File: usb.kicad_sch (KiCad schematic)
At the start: 46 parts, among them J901 AU-Y1008-2-BLK, J902 AU-Y1008-2-BLK, U901 USB2514B/M2, U902 AP22966DC8-7, U903 AP22966DC8-7, U904 USBLC6-2SC6, U905 USBLC6-2SC6, U906 USBLC6-2SC6, U907 USBLC6-2SC6, Y901 24 MHz

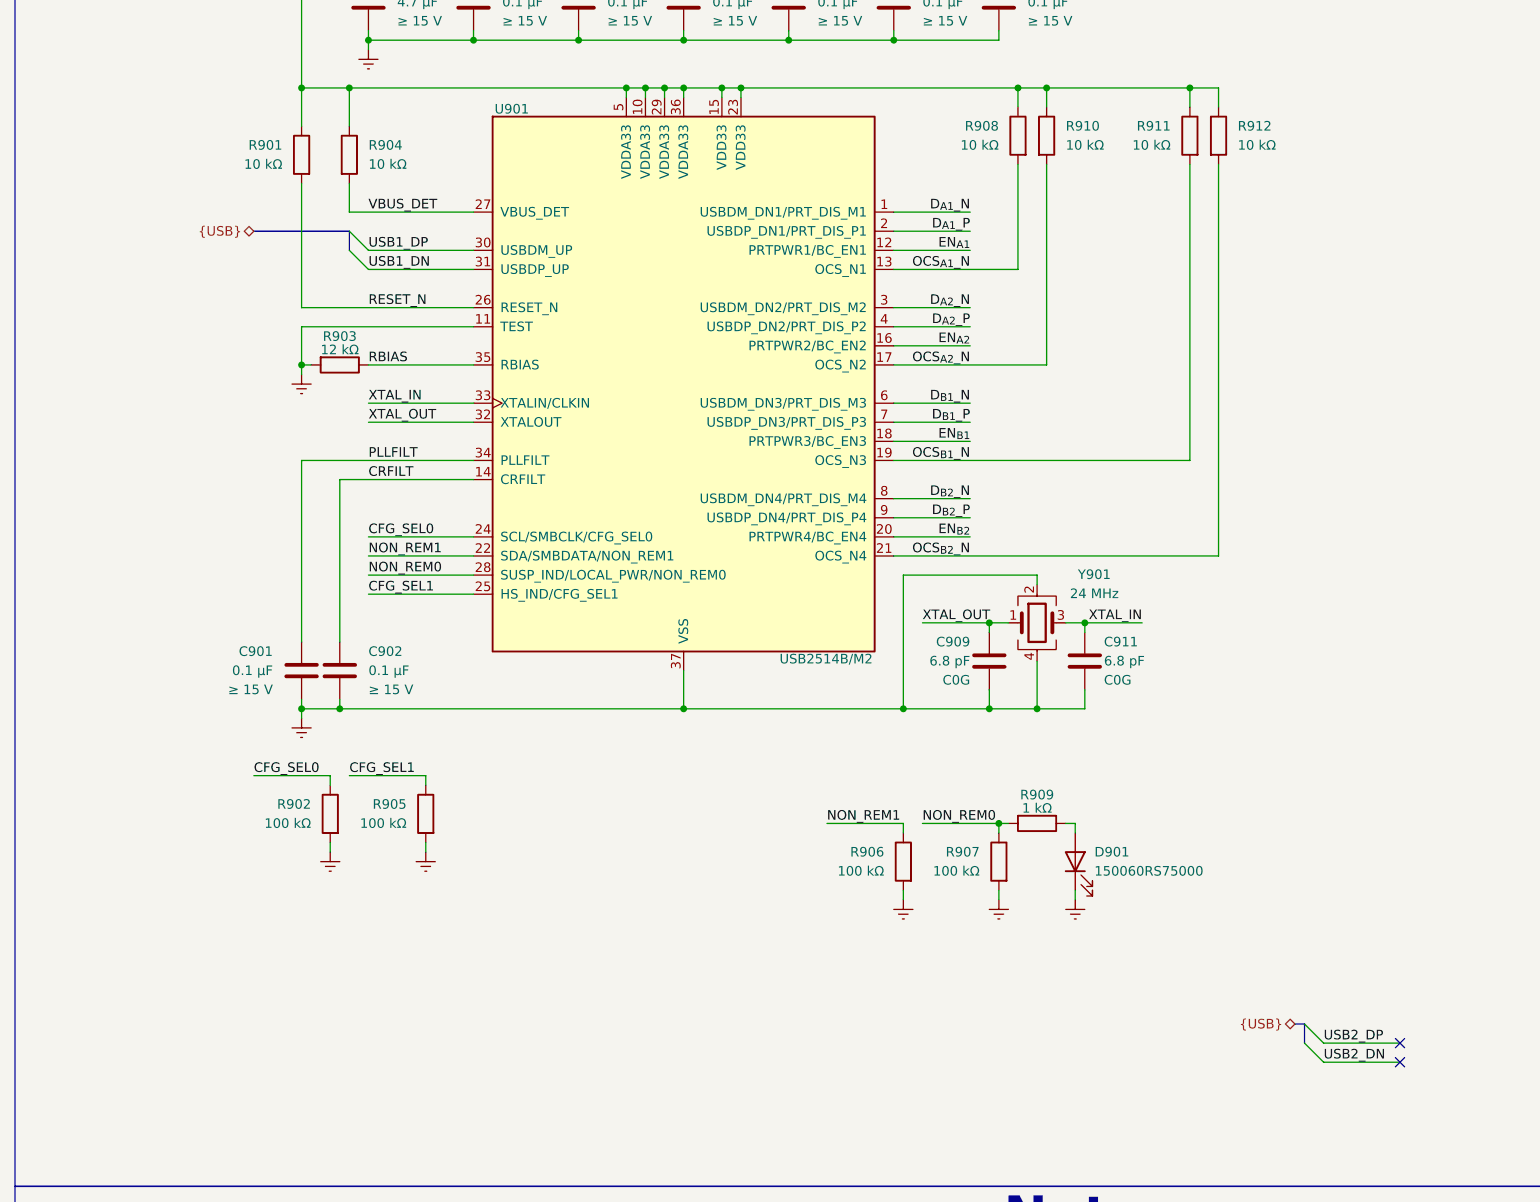
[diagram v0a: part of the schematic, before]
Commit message: Add ETH schema
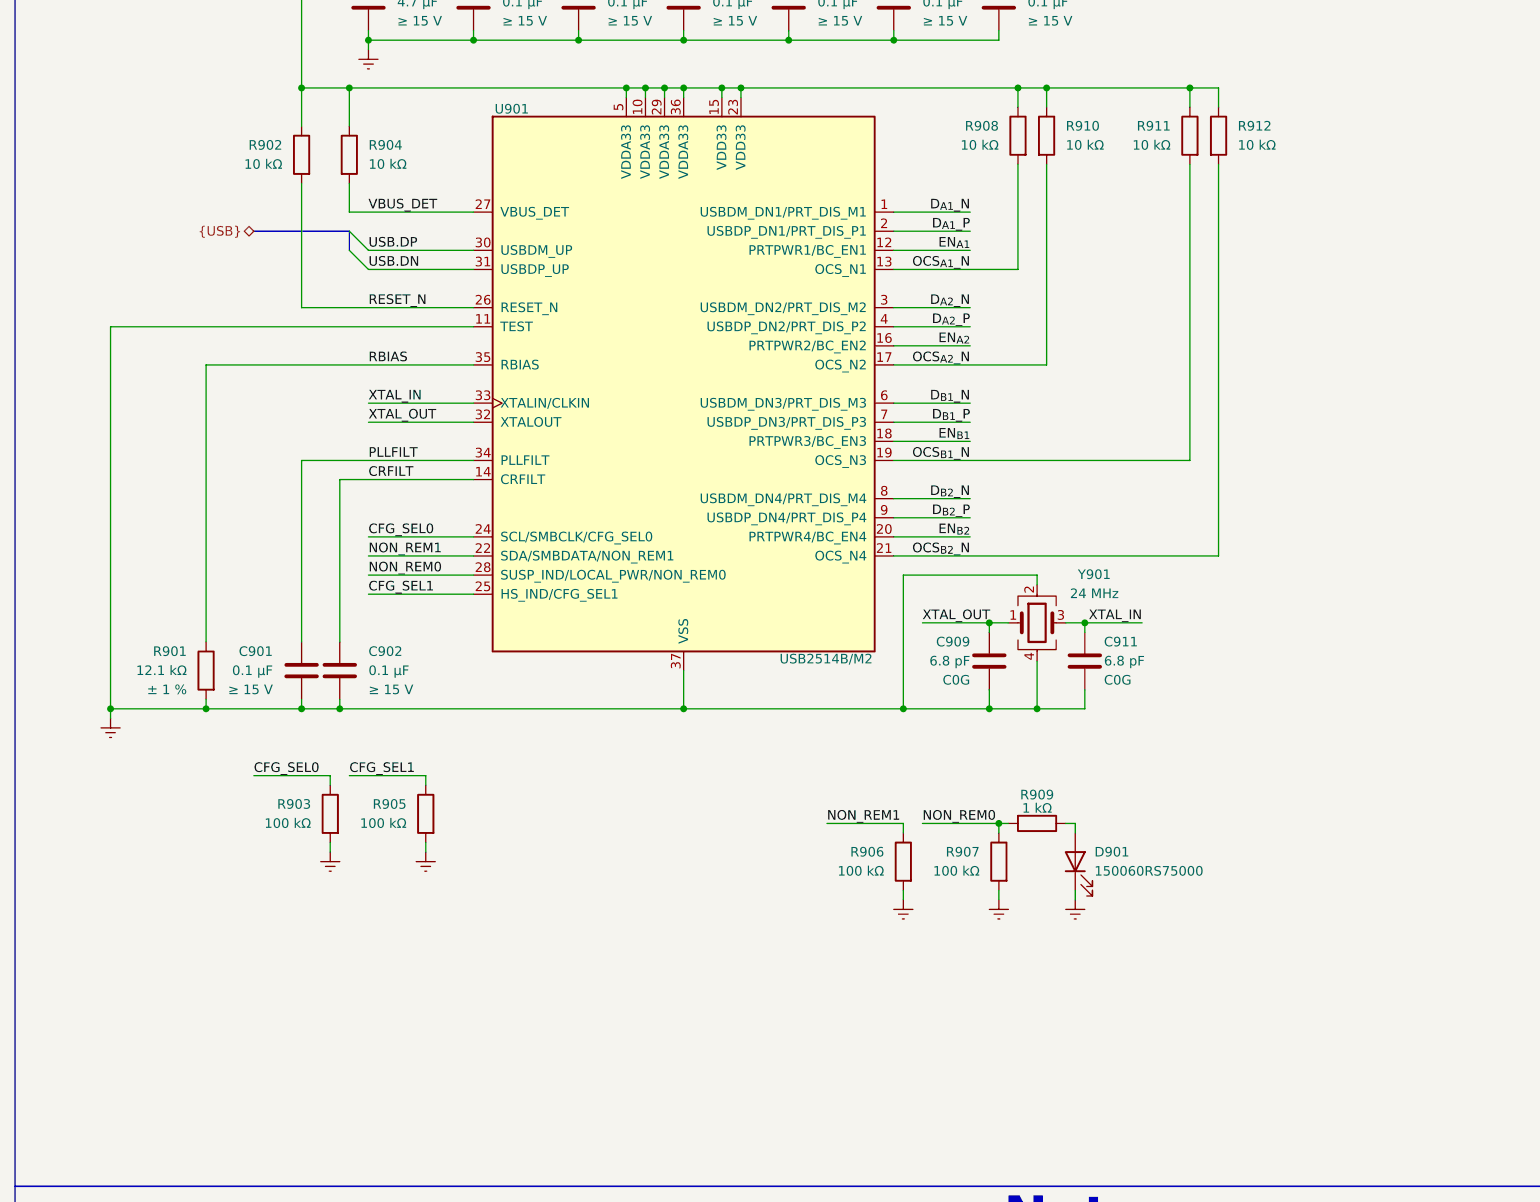
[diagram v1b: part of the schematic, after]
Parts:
- removed R903: 12 kΩ, perfect_footprints:R_0402_1005Metric, symbol Device:R
- added R901: 12.1 kΩ, perfect_footprints:R_0402_1005Metric, symbol Device:R
- renumbered R901 to R902, R902 to R903
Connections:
- net GND: now also R901.2
- net RBIAS: now also R901.1
- net USB1_DN renamed USB.DN
- net USB1_DP renamed USB.DP
- no-connect marks 4 -> 2

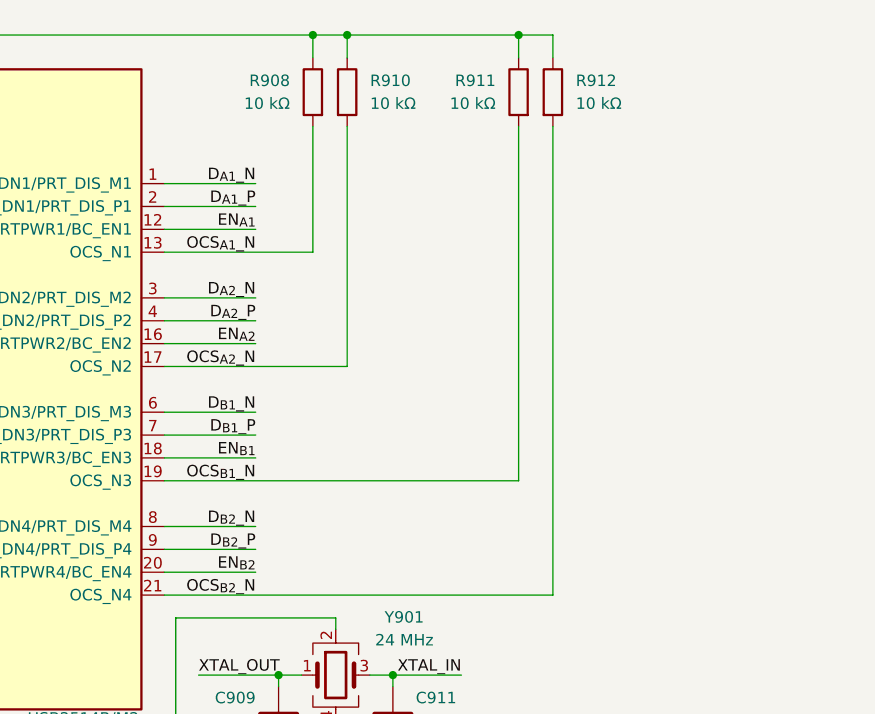
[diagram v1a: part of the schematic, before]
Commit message: Add series termination, assign netclasses, fill schemas' descriptions
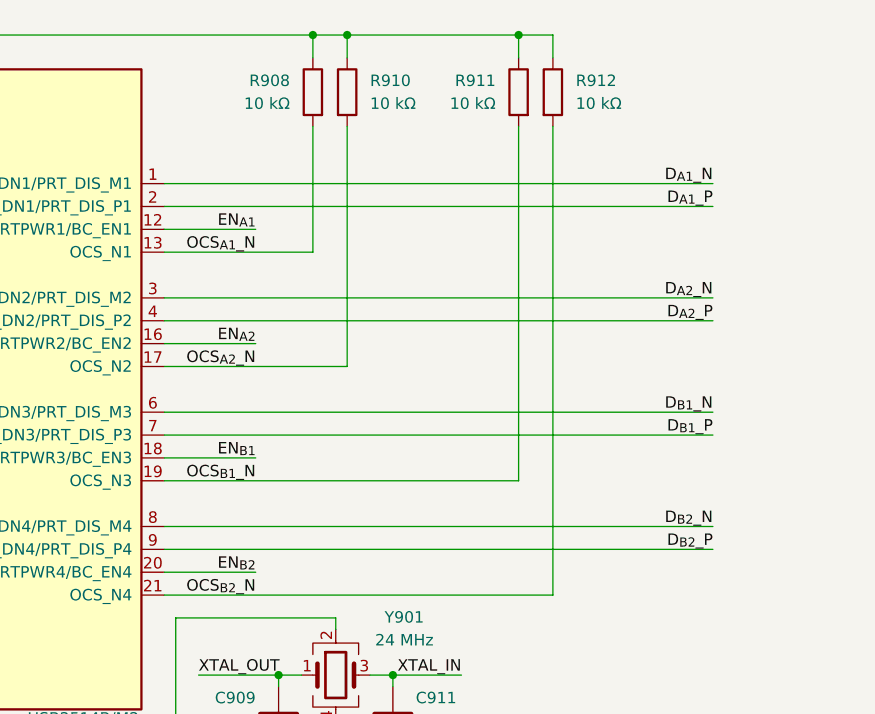
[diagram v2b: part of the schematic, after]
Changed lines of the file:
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@@
 	(wire
 		(pts
-			(xy 129.54 160.02) (xy 139.7 160.02)
+			(xy 129.54 160.02) (xy 190.5 160.02)
 		)
 		(stroke
@@
 	(wire
 		(pts
-			(xy 129.54 149.86) (xy 139.7 149.86)
+			(xy 129.54 149.86) (xy 190.5 149.86)
 		)
 		(stroke
@@
 	(wire
 		(pts
-			(xy 129.54 134.62) (xy 139.7 134.62)
+			(xy 129.54 134.62) (xy 190.5 134.62)
 		)
 		(stroke
@@
 	(wire
 		(pts
-			(xy 129.54 162.56) (xy 139.7 162.56)
+			(xy 129.54 162.56) (xy 190.5 162.56)
 		)
 		(stroke
@@
 	(wire
 		(pts
-			(xy 129.54 124.46) (xy 139.7 124.46)
+			(xy 129.54 124.46) (xy 190.5 124.46)
 		)
 		(stroke
@@
 	(wire
 		(pts
-			(xy 129.54 121.92) (xy 139.7 121.92)
+			(xy 129.54 121.92) (xy 190.5 121.92)
 		)
 		(stroke
@@
 	(wire
 		(pts
-			(xy 129.54 147.32) (xy 139.7 147.32)
+			(xy 129.54 147.32) (xy 190.5 147.32)
 		)
 		(stroke
@@
 	(wire
 		(pts
-			(xy 129.54 137.16) (xy 139.7 137.16)
+			(xy 129.54 137.16) (xy 190.5 137.16)
 		)
 		(stroke
@@
 	)
 	(label "D_{A1}_N"
-		(at 139.7 121.92 180)
+		(at 190.5 121.92 180)
 		(effects
 			(font
@@
 	)
 	(label "D_{B2}_P"
-		(at 139.7 162.56 180)
+		(at 190.5 162.56 180)
 		(effects
 			(font
@@
 	)
 	(label "D_{B2}_N"
-		(at 139.7 160.02 180)
+		(at 190.5 160.02 180)
 		(effects
 			(font
@@
 	)
 	(label "D_{A2}_N"
-		(at 139.7 134.62 180)
+		(at 190.5 134.62 180)
 		(effects
 			(font
@@
 	)
 	(label "D_{B1}_N"
-		(at 139.7 147.32 180)
+		(at 190.5 147.32 180)
 		(effects
 			(font
@@
 	)
 	(label "D_{A1}_P"
-		(at 139.7 124.46 180)
+		(at 190.5 124.46 180)
 		(effects
 			(font
@@
 	)
 	(label "D_{A2}_P"
-		(at 139.7 137.16 180)
+		(at 190.5 137.16 180)
 		(effects
 			(font
@@
 	)
 	(label "D_{B1}_P"
-		(at 139.7 149.86 180)
+		(at 190.5 149.86 180)
 		(effects
 			(font
@@
 		)
 	)
+	(rule_area
+		(polyline
+			(pts
+				(xy 176.53 119.38) (xy 176.53 163.83) (xy 179.07 163.83) (xy 179.07 119.38)
+			)
+			(stroke
+				(width 0)
+				(type dash)
+			)
+			(fill
+				(type none)
+			)
+		)
+	)
+	(rule_area
+		(polyline
+			(pts
+				(xy 347.98 166.37) (xy 347.98 181.61) (xy 350.52 181.61) (xy 350.52 166.37)
+			)
+			(stroke
+				(width 0)
+				(type dash)
+			)
+			(fill
+				(type none)
+			)
+		)
+	)
+	(rule_area
+		(polyline
+			(pts
+				(xy 347.98 118.11) (xy 347.98 133.35) (xy 350.52 133.35) (xy 350.52 118.11)
+			)
+			(stroke
+				(width 0)
+				(type dash)
+			)
+			(fill
+				(type none)
+			)
+		)
+	)
+	(netclass_flag ""
+		(length 2.54)
+		(shape round)
+		(at 349.25 166.37 0)
+		(fields_autoplaced yes)
+		(effects
+			(font
+				(size 1.27 1.27)
+			)
+			(justify left bottom)
+		)
+		(property "Netclass" "USB"
+			(at 349.9485 163.83 0)
+			(effects
+				(font
+					(size 1.27 1.27)
+				)
+				(justify left)
+			)
+		)
+		(property "Component Class" ""
+			(at 257.81 55.88 0)
+			(effects
+				(font
+					(size 1.27 1.27)
+					(italic yes)
+				)
+			)
+		)
+	)
+	(netclass_flag ""
+		(length 2.54)
+		(shape round)
+		(at 177.8 119.38 0)
+		(fields_autoplaced yes)
+		(effects
+			(font
+				(size 1.27 1.27)
+			)
+			(justify left bottom)
+		)
+		(property "Netclass" "USB"
+			(at 178.4985 116.84 0)
+			(effects
+				(font
+					(size 1.27 1.27)
+				)
+				(justify left)
+			)
+		)
+		(property "Component Class" ""
+			(at 86.36 8.89 0)
+			(effects
+				(font
+					(size 1.27 1.27)
+					(italic yes)
+				)
+			)
+		)
+	)
+	(netclass_flag ""
+		(length 2.54)
+		(shape round)
+		(at 45.72 124.46 0)
+		(fields_autoplaced yes)
+		(effects
+			(font
+				(size 1.27 1.27)
+			)
+			(justify left bottom)
+		)
+		(property "Netclass" "USB"
+			(at 46.4185 121.92 0)
+			(effects
+				(font
+					(size 1.27 1.27)
+				)
+				(justify left)
+			)
+		)
+		(property "Component Class" ""
+			(at -45.72 13.97 0)
+			(effects
+				(font
+					(size 1.27 1.27)
+					(italic yes)
+				)
+			)
+		)
+	)
+	(netclass_flag ""
+		(length 2.54)
+		(shape round)
+		(at 349.25 118.11 0)
+		(fields_autoplaced yes)
+		(effects
+			(font
+				(size 1.27 1.27)
+			)
+			(justify left bottom)
+		)
+		(property "Netclass" "USB"
+			(at 349.9485 115.57 0)
+			(effects
+				(font
+					(size 1.27 1.27)
+				)
+				(justify left)
+			)
+		)
+		(property "Component Class" ""
+			(at 257.81 7.62 0)
+			(effects
+				(font
+					(size 1.27 1.27)
+					(italic yes)
+				)
+			)
+		)
+	)

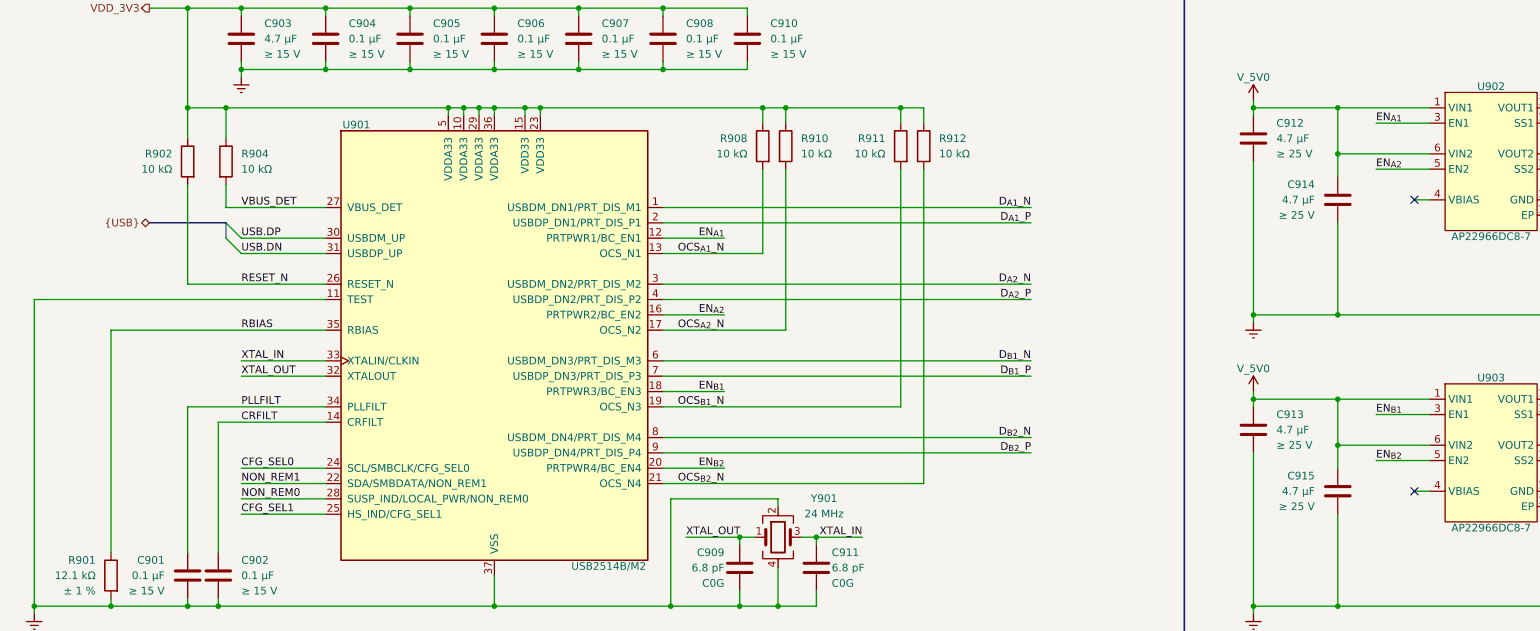
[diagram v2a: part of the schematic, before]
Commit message: Add test points, assign netclasses and clean-up
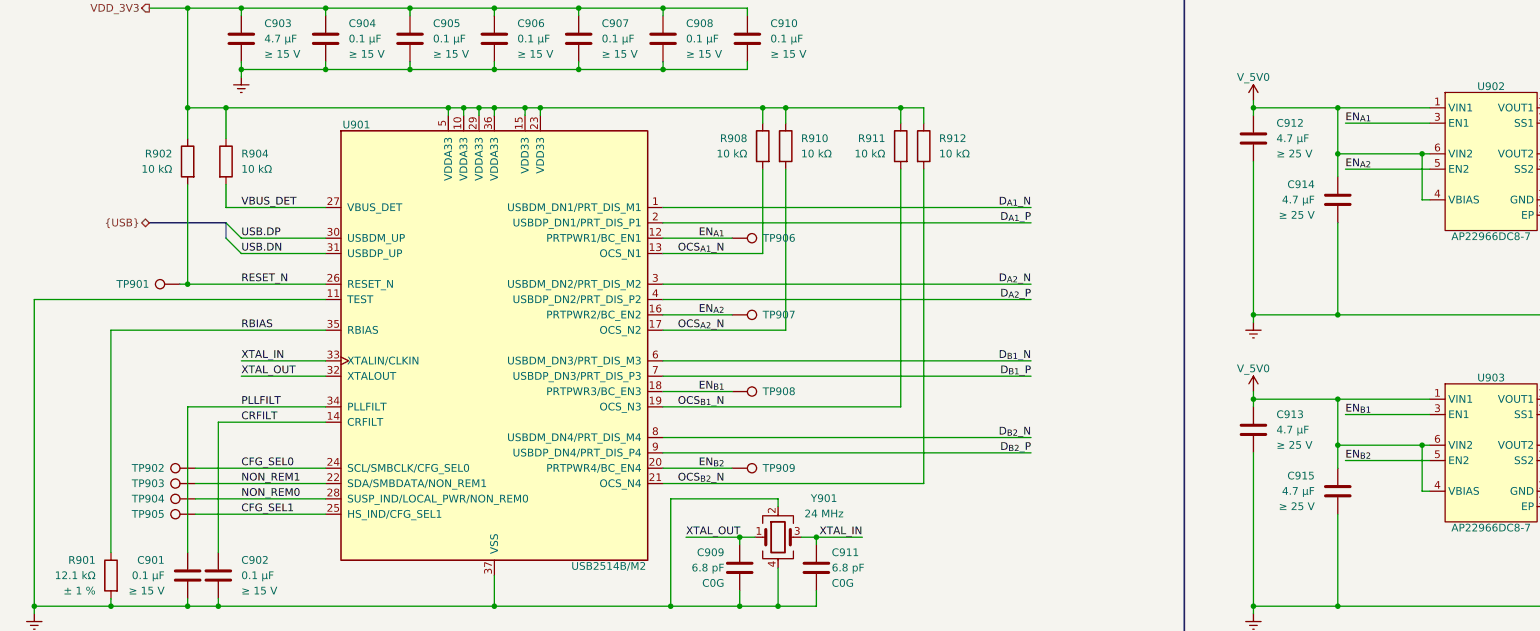
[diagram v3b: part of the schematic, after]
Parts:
- added TP901, TP902, TP903, TP904, TP905, TP906, TP907, TP908, TP909: TestPoint, TestPoint:TestPoint_Pad_D1.0mm, symbol Connector:TestPoint
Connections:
- net CFG_SEL0: now also TP902.1
- net CFG_SEL1: now also TP905.1
- net EN_{A1}: now also TP906.1
- net EN_{A2}: now also TP907.1
- net EN_{B1}: now also TP908.1
- net EN_{B2}: now also TP909.1
- net NON_REM0: now also TP904.1
- net NON_REM1: now also TP903.1
- net RESET_N: now also TP901.1
- net V_5V0: now also U902.4 (VBIAS), U903.4 (VBIAS)
- no-connect marks 2 -> 0

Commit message: Refactor symbol properties
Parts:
- D901: DigiKey Part Number 732-4978-1-ND -> (none)
- R902, R904, R908, R909, R910, R911, R912: DigiKey Part Number 732-560112110020CT-ND -> (none)
- R903, R905, R906, R907: DigiKey Part Number 732-560112110019CT-ND -> (none)
- Y901: footprint MountingHole:MountingHole_2.2mm_M2_DIN965_Pad -> (none)
